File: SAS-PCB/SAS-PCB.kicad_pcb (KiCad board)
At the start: 2 copper layers, 76.2 x 76.2 mm, 25 parts, among them J10-FTDI1 Conn_01x06, J10-FTDI2 Conn_01x06, J1_Batt1 691137710002, J2-LCD1 Conn_01x04_Socket, J3-LCD2 Conn_01x04_Socket, J4-BMP280 Conn_01x06_Pin, J5-GPS1 Conn_01x04_Socket, J6-cable-plat1 Conn_02x20_Odd_Even, J7-RFD900x1 691137710002, J8-Fan1 Conn_01x04_Socket, J9-Fan2 Conn_01x04_Socket

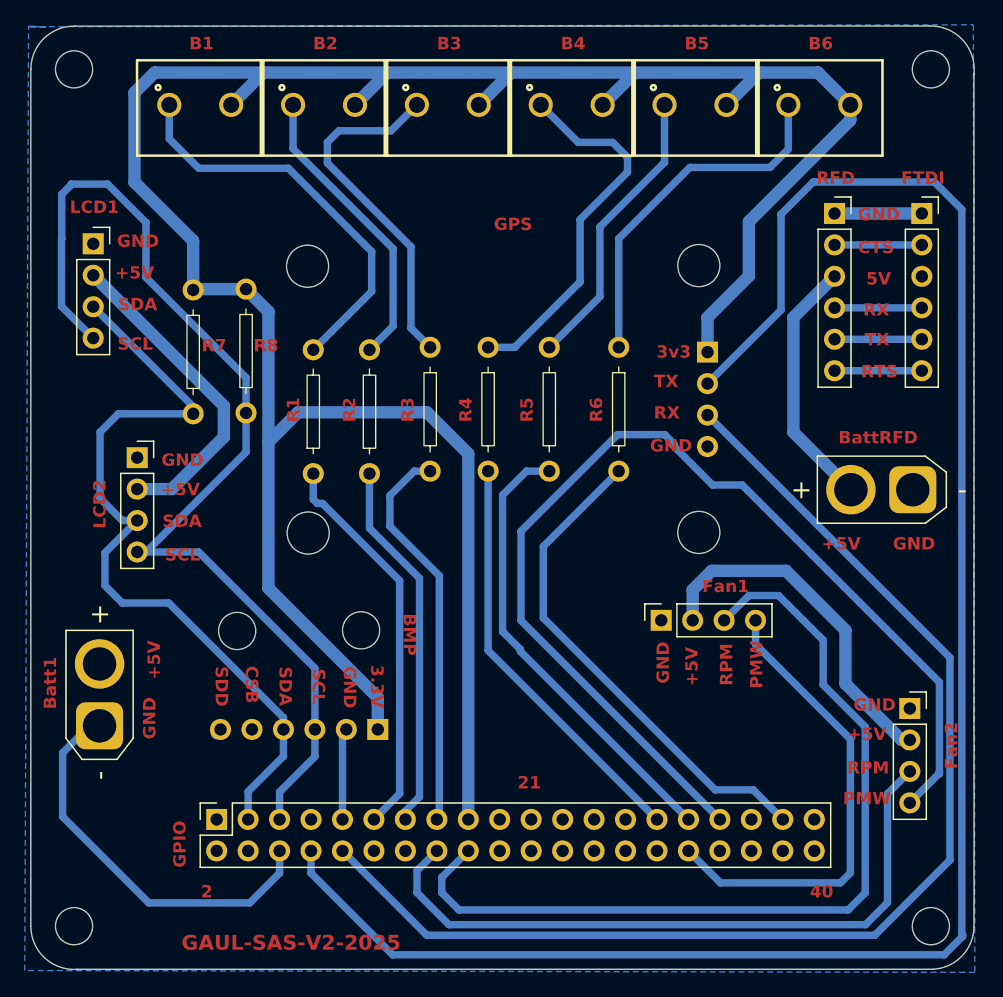
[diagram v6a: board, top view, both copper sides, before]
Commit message: Version_préliminaire
version préliminaire: fil jumper nécessaire pour certaines connections(moins de 5)
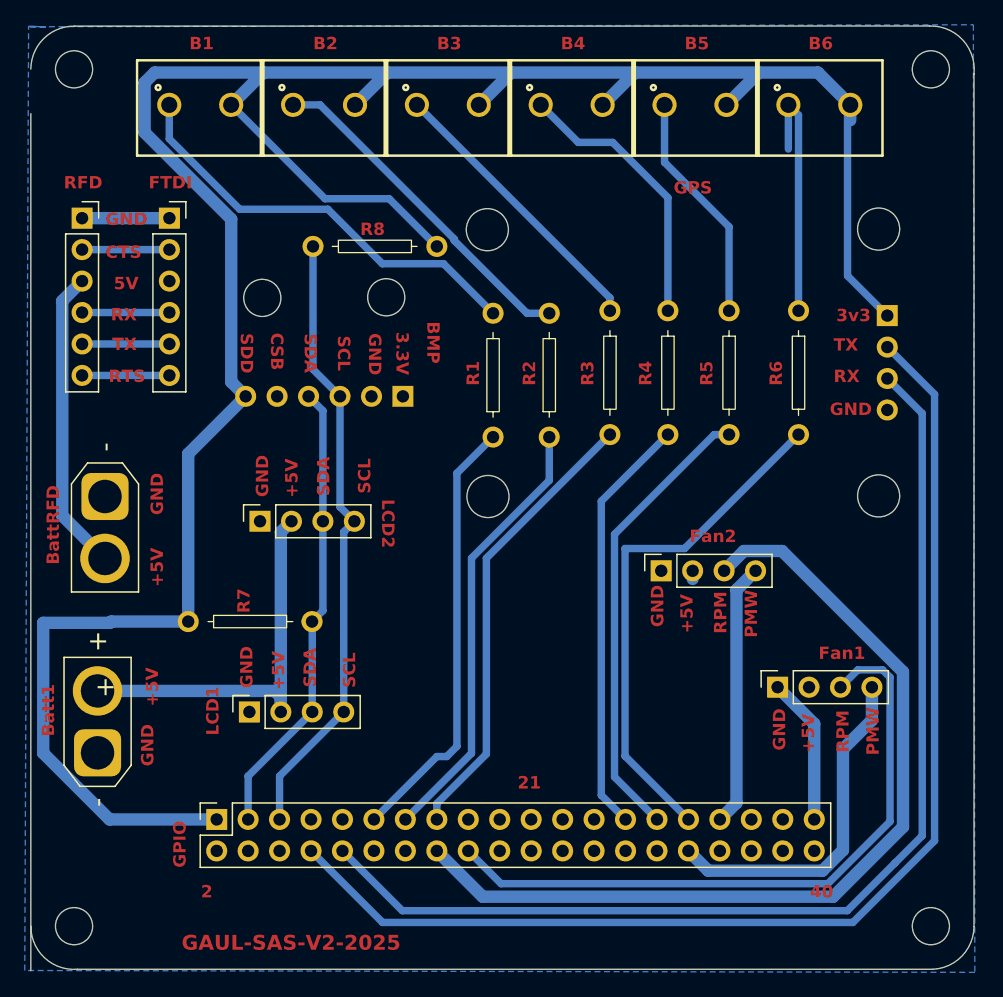
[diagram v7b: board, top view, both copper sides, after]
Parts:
- moved J7-RFD900x1 65.2 mm to (66.0, 98.0), turned to -90 degrees
- moved J10-FTDI1 60.8 mm to (71.1, 92.9)
- moved J10-FTDI2 60.8 mm to (64.0, 92.9)
- moved J2-LCD1 44.7 mm to (87.1, 121.7), turned to 90 degrees
- moved J4-BMP280 27.0 mm to (77.4, 89.9)
- moved J3-LCD2 25.6 mm to (87.9, 106.2), turned to 90 degrees
- moved R7 22.3 mm to (77.8, 108.2), turned to 0 degrees
- moved J9-Fan2 14.9 mm to (120.3, 110.2), turned to 90 degrees
- moved J5-GPS1 14.8 mm to (129.2, 87.2)
- moved R2 14.8 mm to (102.0, 88.1)
- moved R3 14.8 mm to (106.7, 88.1)
- moved R1 14.8 mm to (97.4, 88.1)
- moved R4 14.8 mm to (111.4, 88.1)
- moved R5 14.8 mm to (116.3, 88.1)
- moved R6 14.8 mm to (121.9, 88.1)
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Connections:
- J6-cable-plat1 pad 27: unconnected-(J6-cable-plat1-Pin_27-Pad27) -> Bouton_4
- J6-cable-plat1 pad 29: Bouton_4 -> Bouton_5
- J6-cable-plat1 pad 31: Bouton_5 -> Bouton_6
- J6-cable-plat1 pad 37: Bouton_6 -> unconnected-(J6-cable-plat1-Pin_37-Pad37)
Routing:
- net Fan2_PWM: track 86.4 -> 21.3 mm
- net TXD: track 149.4 -> 97.1 mm
- net SCL: track 86.8 -> 50.2 mm
- net GND: track 46.7 -> 20.2 mm
- net SDA: track 63.9 -> 37.9 mm
- net Fan2_RPM: track 55.2 -> 73.5 mm
- net Fan1_RPM: track 71.8 -> 53.7 mm
- net +5V: track 75.9 -> 58.3 mm
- net Fan1_PWM: track 38.1 -> 28.0 mm
- net RXD: track 98.4 -> 89.4 mm
- net Net-(Bouton_6-GND): track 29.0 -> 20.5 mm
- net +3.3V: track 213.5 -> 205.2 mm
- net Net-(Bouton_4-GND): track 30.0 -> 22.5 mm
- net Bouton_2: track 30.1 -> 35.7 mm
- net Net-(Bouton_3-GND): track 28.5 -> 23.1 mm
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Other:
- board size 76.2 x 76.2 mm -> 76.2 x 76.3 mm

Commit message: Corrections mineures
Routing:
- net +3.3V: track 205.2 -> 203.7 mm
- net SDA: track 37.9 -> 37.3 mm
- added copper zone on F.Cu, net (none)
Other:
- board size 76.2 x 76.3 mm -> 76.2 x 76.2 mm
